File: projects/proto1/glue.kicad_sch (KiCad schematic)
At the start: 11 parts, among them U48 PAL16L8, U49 EPM7128SLC84-15, U50 PAL16L8

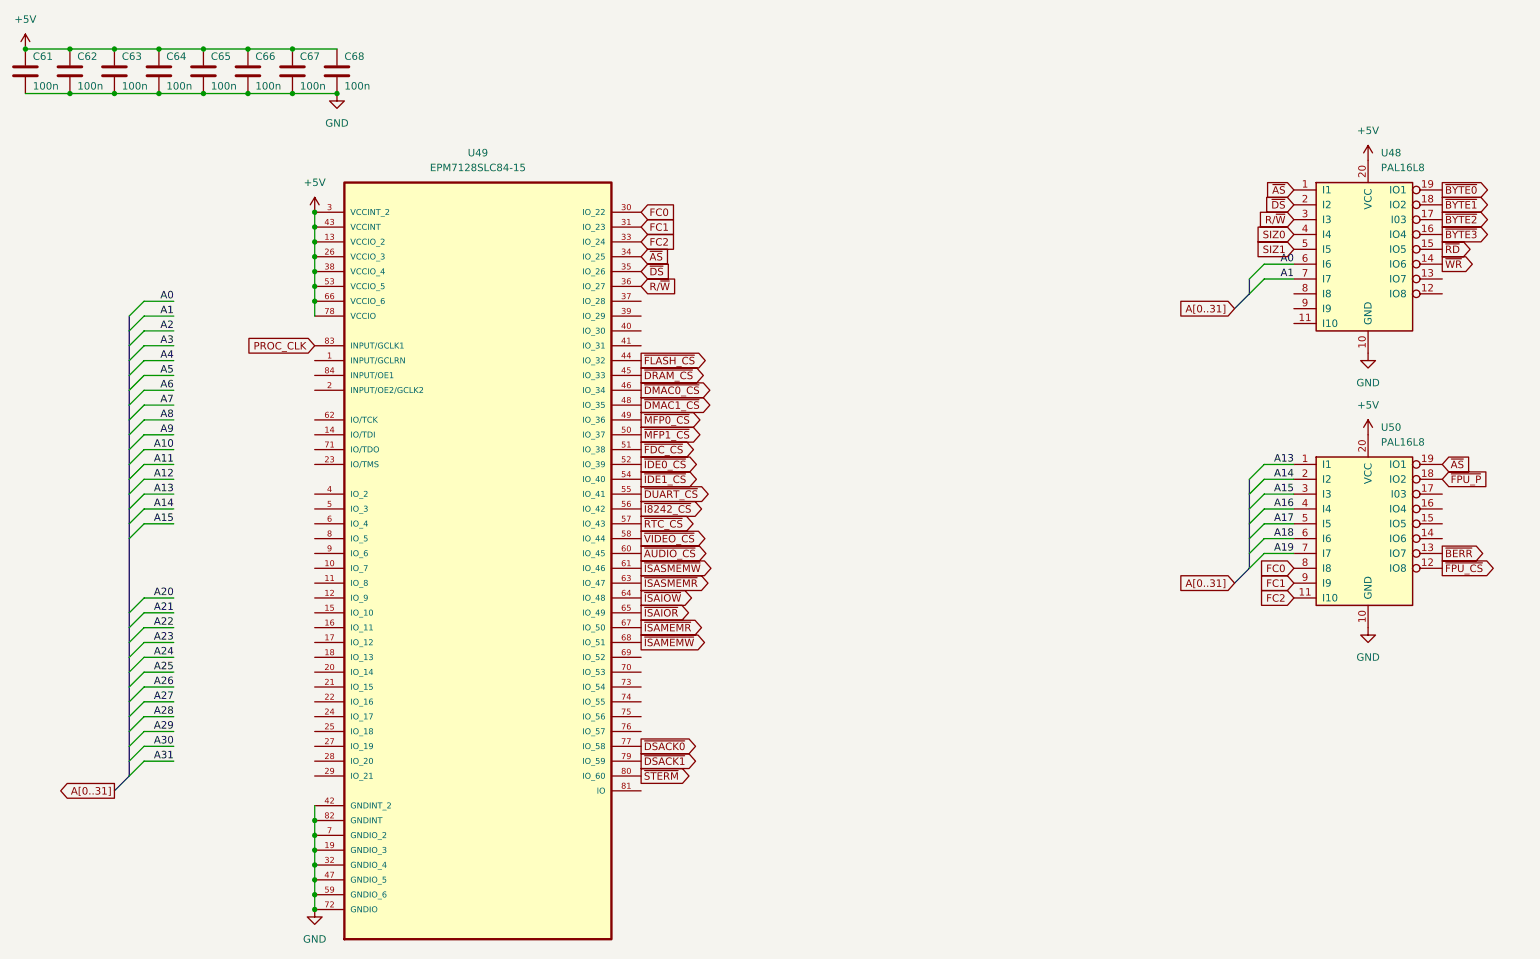
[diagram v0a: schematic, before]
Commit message: Renamed CMC to SCU, changed verification method to cocotb, and modified pcb schematic
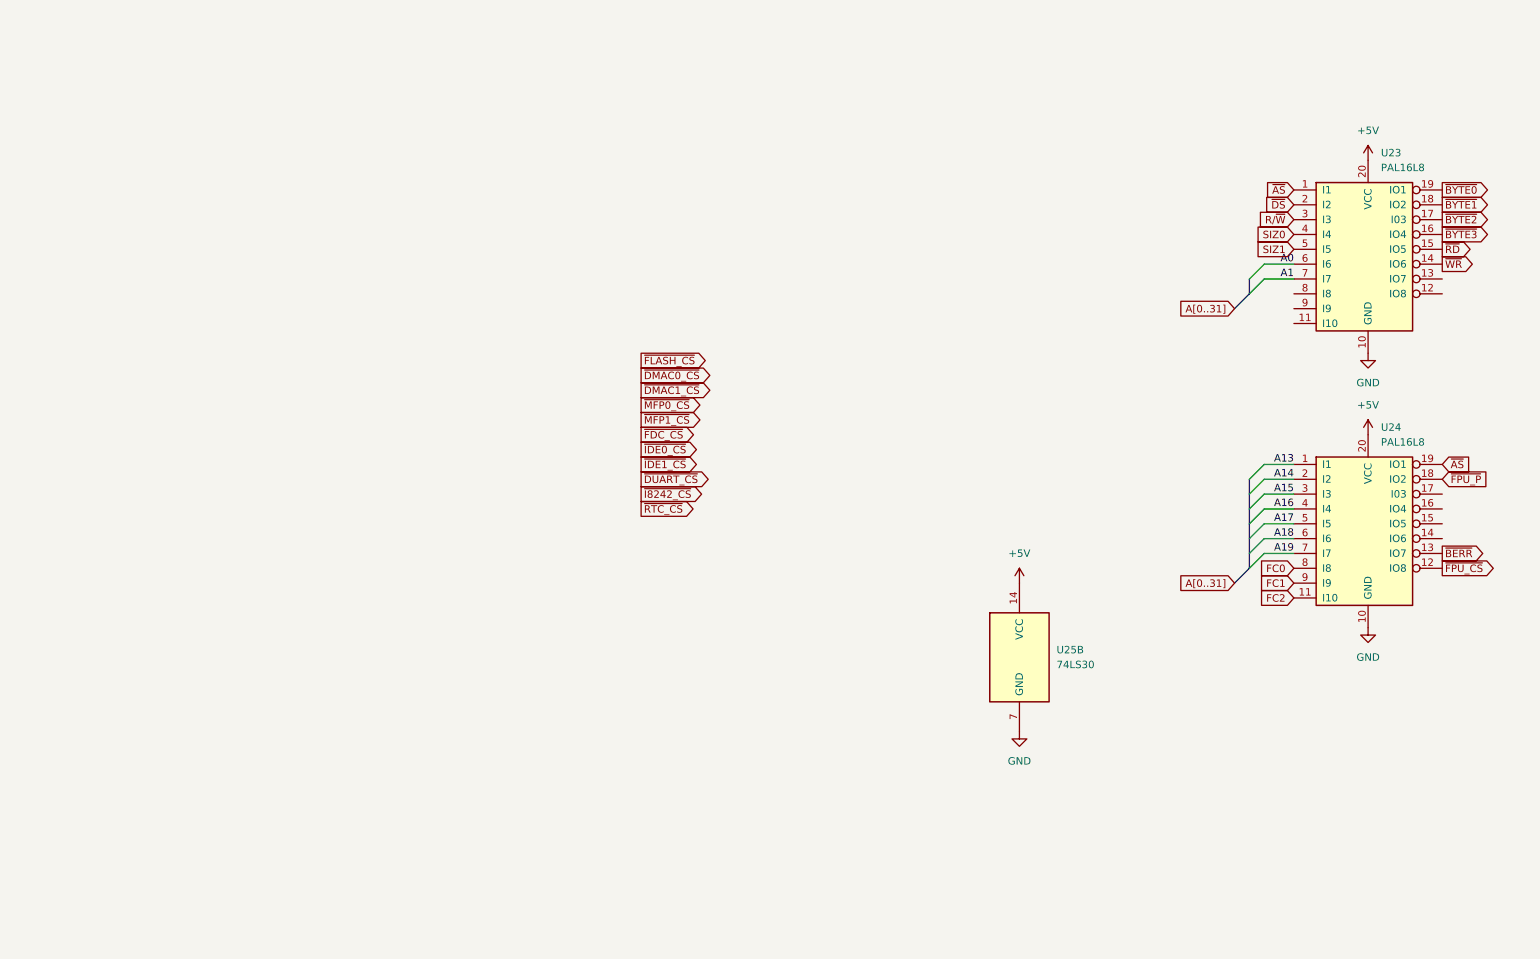
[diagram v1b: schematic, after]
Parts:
- removed C61, C62, C63, C64, C65, C66, C67, C68: 100n, Capacitor_THT:C_Disc_D4.3mm_W1.9mm_P5.00mm, symbol Device:C
- removed U49: EPM7128SLC84-15, Package_LCC:PLCC-84_THT-Socket, symbol EPM7128SLC84-15:EPM7128SLC84-15
- added U25: 74LS30, symbol 74xx:74LS30
- renumbered U48 to U23, U50 to U24
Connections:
- net +5V: now also U25.14 (VCC)
- net GND: now also U25.7 (GND)
